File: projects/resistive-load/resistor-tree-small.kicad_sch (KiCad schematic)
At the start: 27 parts, among them Q35 SSM3K333R, Q36 SSM3K333R, Q37 SSM3K333R, Q38 SSM3K333R, Q39 SSM3K333R

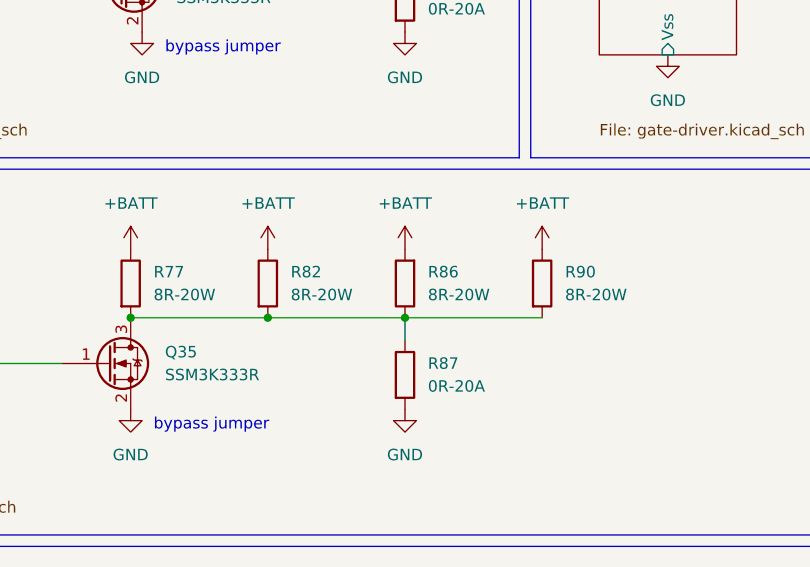
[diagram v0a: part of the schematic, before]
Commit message: fix: update pin assignment for transistors
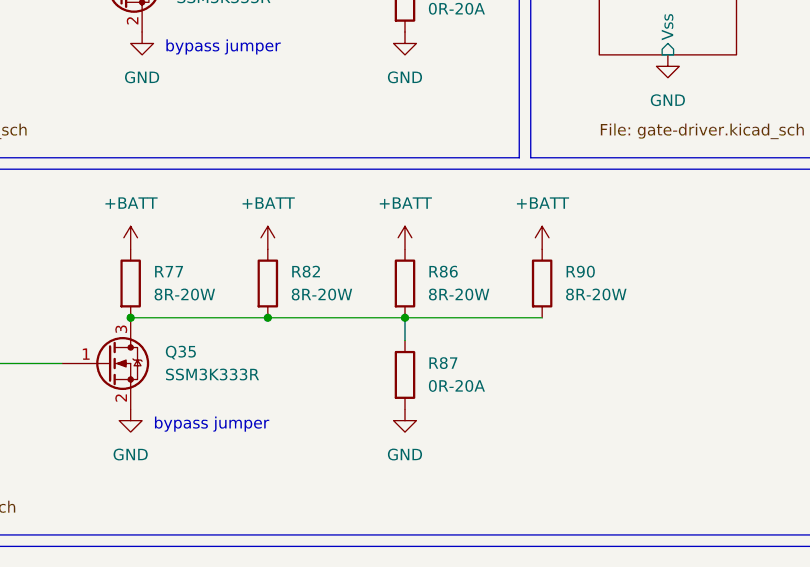
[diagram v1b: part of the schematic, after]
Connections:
- net +BATT: now also R86.1; no longer R86.2
- net at Q35.3 (D), R77.2, R82.2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: now also R86.2; no longer R86.1
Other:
- moved on the sheet: R86

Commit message: Ayo
Ayo
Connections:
- net +BATT: now also R86.2; no longer R86.1
- net at Q35.3 (D), R77.2, R82.2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: now also R86.1; no longer R86.2
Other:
- moved on the sheet: R86
